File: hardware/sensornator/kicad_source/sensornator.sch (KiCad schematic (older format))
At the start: 50 parts, among them CN1 ARDUINO, CON1 Micro_SDCard, P1 USB_OTG, Q1 2N7002, Q2 2N7002, SW1 TAST_VER, SW2 TAST_VER, U1 TPS383X, U2 MCP73831, U3 TPS736XX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

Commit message: updated schematic, added extra pages for history and usb, added esp32 reset circuit
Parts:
- removed BT1: Battery, MECH_battery_holder:KEYSTONE_1043, symbol devices:Battery
- removed C1, C2, C7: 1u, capacitors:C_0603, symbol devices:C_0603
- removed C3, C5: 10u, capacitors:C_0603, symbol devices:C_0603
- removed C4, C6: 100n, capacitors:C_0603, symbol devices:C_0603
- removed D1, D3, D4: green, LEDs:LED_0603, symbol devices:Led_Small
- removed F1: F_Small, fuse_holders_and_fuses:Fuse_SMD1206_Reflow, symbol devices:F_Small
- removed P1: USB_OTG, mechanical-connectors:USB_Micro-B, symbol mechanical-connectors:USB_OTG
- removed Q1, Q2: 2N7002, SOT_TO:SOT-23, symbol devices:Q_NMOS_GSD
- removed R1, R10, R6, R9: 1k, resistors:R_0603, symbol devices:R_1206
- removed R16, R17: 100R, resistors:R_0603, symbol devices:R_1206
- removed R3: 22k1, resistors:R_0603, symbol devices:R_1206
- removed R4: 47k5, resistors:R_0603, symbol devices:R_1206
- removed R5: 10k, resistors:R_0603, symbol devices:R_1206
- removed R7: 2k5, resistors:R_0603, symbol devices:R_1206
- removed U1: TPS383X, SOT_TO:SOT-23, symbol IC_voltage_supervisor:TPS383X
- removed U2: MCP73831, SOT_TO:SOT-23-5, symbol IC_batterycharger:MCP73831
- removed U3: TPS736XX, SOT_TO:SOT-23-5, symbol voltage-regulators:TPS736XX
- removed U4: CP2102N_28, QFN:QFN-28-1EP_5x5mm_Pitch0.5mm, symbol IC_interface_usb:CP2102N_28
- D2: value green -> blue
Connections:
- net labels removed: CHR_100MA, CHR_500MA, PROG, RX_R, TX_R, VIN, VIO
- wire segments 246 -> 139
- no-connect marks 26 -> 11
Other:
- note removed: "do not connect pin 4!!!"
- note removed: "use MCP73832-2ACI/OT (4.2 V)"
- note removed: "use TPS3839G33DBZR\nthreshold voltage 3.08 V"
- note removed: "use TPS73630DBVT\nfixed voltage 3.0 V"

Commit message: changed micro SD card socket to push pull type, updated footprint of micro USB socket
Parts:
- CON1: footprint CON_wuerth:WE_693072010801 -> CON_wuerth:WE_693071010811
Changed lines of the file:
@@
 F 0 "CON1" H 6327 7128 50  0000 L CNN
 F 1 "Micro_SDCard" H 6327 7030 59  0000 L CNN
-F 2 "CON_wuerth:WE_693072010801" H 5550 7300 50  0000 C CNN
+F 2 "CON_wuerth:WE_693071010811" H 5550 7300 50  0001 C CNN
 F 3 "" H 5350 6950 60  0000 C CNN
 	1    5150 6950

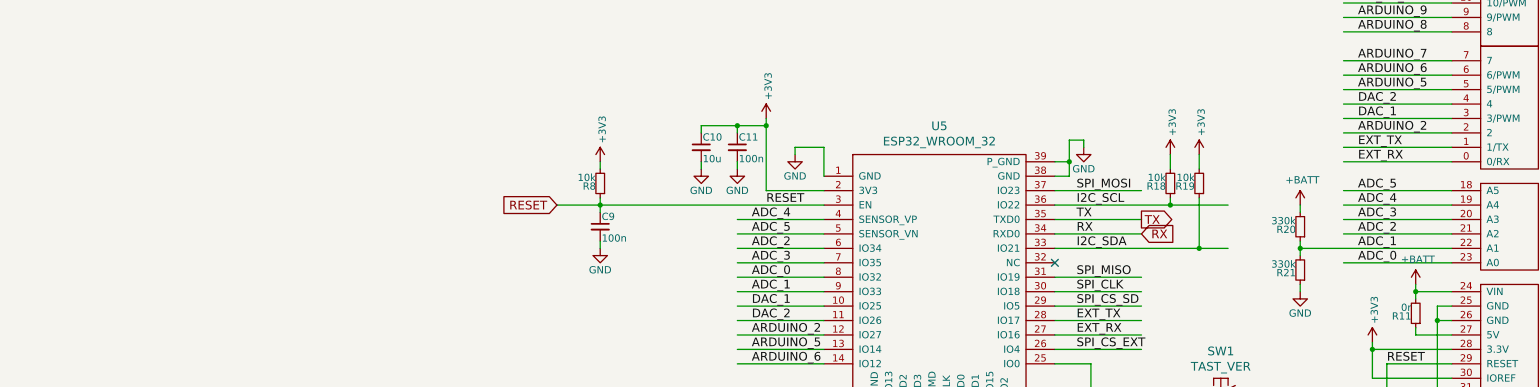
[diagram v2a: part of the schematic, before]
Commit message: updated schematic, added USB voltage bypass, finished layout, corrected 3D models
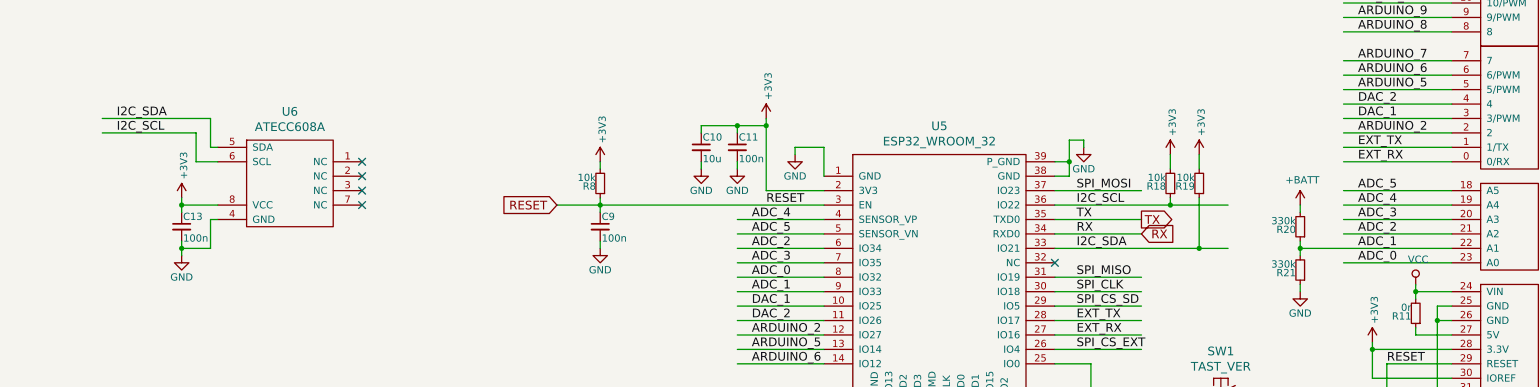
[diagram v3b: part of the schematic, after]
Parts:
- added C13: 100n, capacitors:C_0603, symbol devices:C_0603
- added U6: ATECC608A, SOIC:SOIC-8_3.9x4.9mm_Pitch1.27mm, symbol IC_interface_i2c:ATECC608A
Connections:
- net labels added: VCC
- wire segments 139 -> 153
- no-connect marks 11 -> 15
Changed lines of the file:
@@
 Text Label 9850 3950 0    60   ~ 0
 ADC_1
-$Comp
-L power-supply:+BATT #PWR044
-U 1 1 5C3F862C
-P 10250 4200
-F 0 "#PWR044" H 10250 4050 50  0001 C CNN
-F 1 "+BATT" H 10265 4373 50  0000 C CNN
-F 2 "" H 10250 4200 50  0000 C CNN
-F 3 "" H 10250 4200 50  0000 C CNN
-	1    10250 4200
-	1    0    0    -1
-$EndComp
 Wire Wire Line
 	5550 4550 6150 4550
@@
 	8000 5350 8000 5100
 Connection ~ 8000 5100
+$Comp
+L IC_interface_i2c:ATECC608A U6
+U 1 1 5CB3A3E7
+P 2450 3850
+F 0 "U6" H 2450 4697 60  0000 C CNN
+F 1 "ATECC608A" H 2450 4591 60  0000 C CNN
+F 2 "SOIC:SOIC-8_3.9x4.9mm_Pitch1.27mm" H 3050 3700 60  0001 C CNN
+F 3 "" H 3050 3700 60  0001 C CNN
+	1    2450 3850
+	1    0    0    -1
+$EndComp
+NoConn ~ 2950 3350
+NoConn ~ 2950 3450
+NoConn ~ 2950 3550
+NoConn ~ 2950 3650
+$Comp
+L devices:C_0603 C13
+U 1 1 5CB511EF
+P 1700 3800
+F 0 "C13" H 1710 3870 50  0000 L CNN
+F 1 "100n" H 1710 3720 50  0000 L CNN
+F 2 "capacitors:C_0603" H 1700 3650 50  0001 C CNN
+F 3 "" H 1700 3800 50  0000 C CNN
+	1    1700 3800
+	1    0    0    -1
+$EndComp
+$Comp
+L power-supply:+3V3 #PWR02
+U 1 1 5CB512AB
+P 1700 3600
+F 0 "#PWR02" H 1700 3450 50  0001 C CNN
+F 1 "+3V3" V 1715 3728 50  0000 L CNN
+F 2 "" H 1700 3600 50  0000 C CNN
+F 3 "" H 1700 3600 50  0000 C CNN
+	1    1700 3600
+	1    0    0    -1
+$EndComp
+$Comp
+L power-supply:GND #PWR03
+U 1 1 5CB512E4
+P 1700 4000
+F 0 "#PWR03" H 1700 3750 50  0001 C CNN
+F 1 "GND" H 1700 3850 50  0000 C CNN
+F 2 "" H 1700 4000 50  0000 C CNN
+F 3 "" H 1700 4000 50  0000 C CNN
+	1    1700 4000
+	1    0    0    -1
+$EndComp
+Wire Wire Line
+	1700 3900 1700 3950
+Wire Wire Line
+	1700 3700 1700 3650
+Wire Wire Line
+	1700 3650 1950 3650
+Connection ~ 1700 3650
+Wire Wire Line
+	1700 3650 1700 3600
+Wire Wire Line
+	1950 3750 1900 3750
+Wire Wire Line
+	1900 3750 1900 3950
+Wire Wire Line
+	1900 3950 1700 3950
+Connection ~ 1700 3950
+Wire Wire Line
+	1700 3950 1700 4000
+Wire Wire Line
+	1150 3150 1800 3150
+Wire Wire Line
+	1800 3150 1800 3350
+Wire Wire Line
+	1800 3350 1950 3350
+Wire Wire Line
+	1150 3050 1900 3050
+Wire Wire Line
+	1900 3050 1900 3250
+Wire Wire Line
+	1900 3250 1950 3250
+Text Label 1250 3050 0    60   ~ 0
+I2C_SDA
+Text Label 1250 3150 0    60   ~ 0
+I2C_SCL
+$Comp
+L power-supply:VCC #PWR0123
+U 1 1 5CBA2F63
+P 10250 4200
+F 0 "#PWR0123" H 10250 4050 50  0001 C CNN
+F 1 "VCC" H 10267 4373 50  0000 C CNN
+F 2 "" H 10250 4200 50  0000 C CNN
+F 3 "" H 10250 4200 50  0000 C CNN
+	1    10250 4200
+	1    0    0    -1
+$EndComp
 $EndSCHEMATC

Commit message: added silk screen on back side, updated parameters, generated pdf schematic
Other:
- note added: "Copyright generationmake 2019\nsee full project documentation at http://sensornator.generationmake.de"
- note removed: "Arduino Uno: SCK=13 MOSI=11\nArduino Leonardo: no spi\nArduino Mega: no spi\nArduino M0 pro: SCK=13 MOSI=11\nArduino Zero: SCK=13 MOSI=11\n\n"
- note removed: "Copyright generationmake 2018\nsee full project documentation at http://ardutrx.generationmake.de"
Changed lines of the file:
@@
 encoding utf-8
 Sheet 1 3
-Title "esp32 arduino"
-Date "2018-12-12"
-Rev "1.0"
+Title "Sensornator"
+Date "2019-04-12"
+Rev "1.1"
 Comp "generationmake"
 Comment1 ""
@@
 ADC_0
 Text Notes 500  650  0    47   ~ 0
-Copyright generationmake 2018\nsee full project documentation at http://ardutrx.generationmake.de
+Copyright generationmake 2019\nsee full project documentation at http://sensornator.generationmake.de
 Wire Wire Line
 	10500 4350 10400 4350
@@
 Wire Wire Line
 	8550 5900 8550 6000
-Text Notes 9150 1300 0    60   ~ 0
-Arduino Uno: SCK=13 MOSI=11\nArduino Leonardo: no spi\nArduino Mega: no spi\nArduino M0 pro: SCK=13 MOSI=11\nArduino Zero: SCK=13 MOSI=11\n\n
 Text Label 9850 2850 0    60   ~ 0
 ARDUINO_5
